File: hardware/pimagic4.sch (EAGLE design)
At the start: 49 parts, among them IC1 ATMEGA328-P, Q1 2N7000, Q2 2N7000, U2 ARDUINO_SHIELDLONGPADS, Y1 16MHz

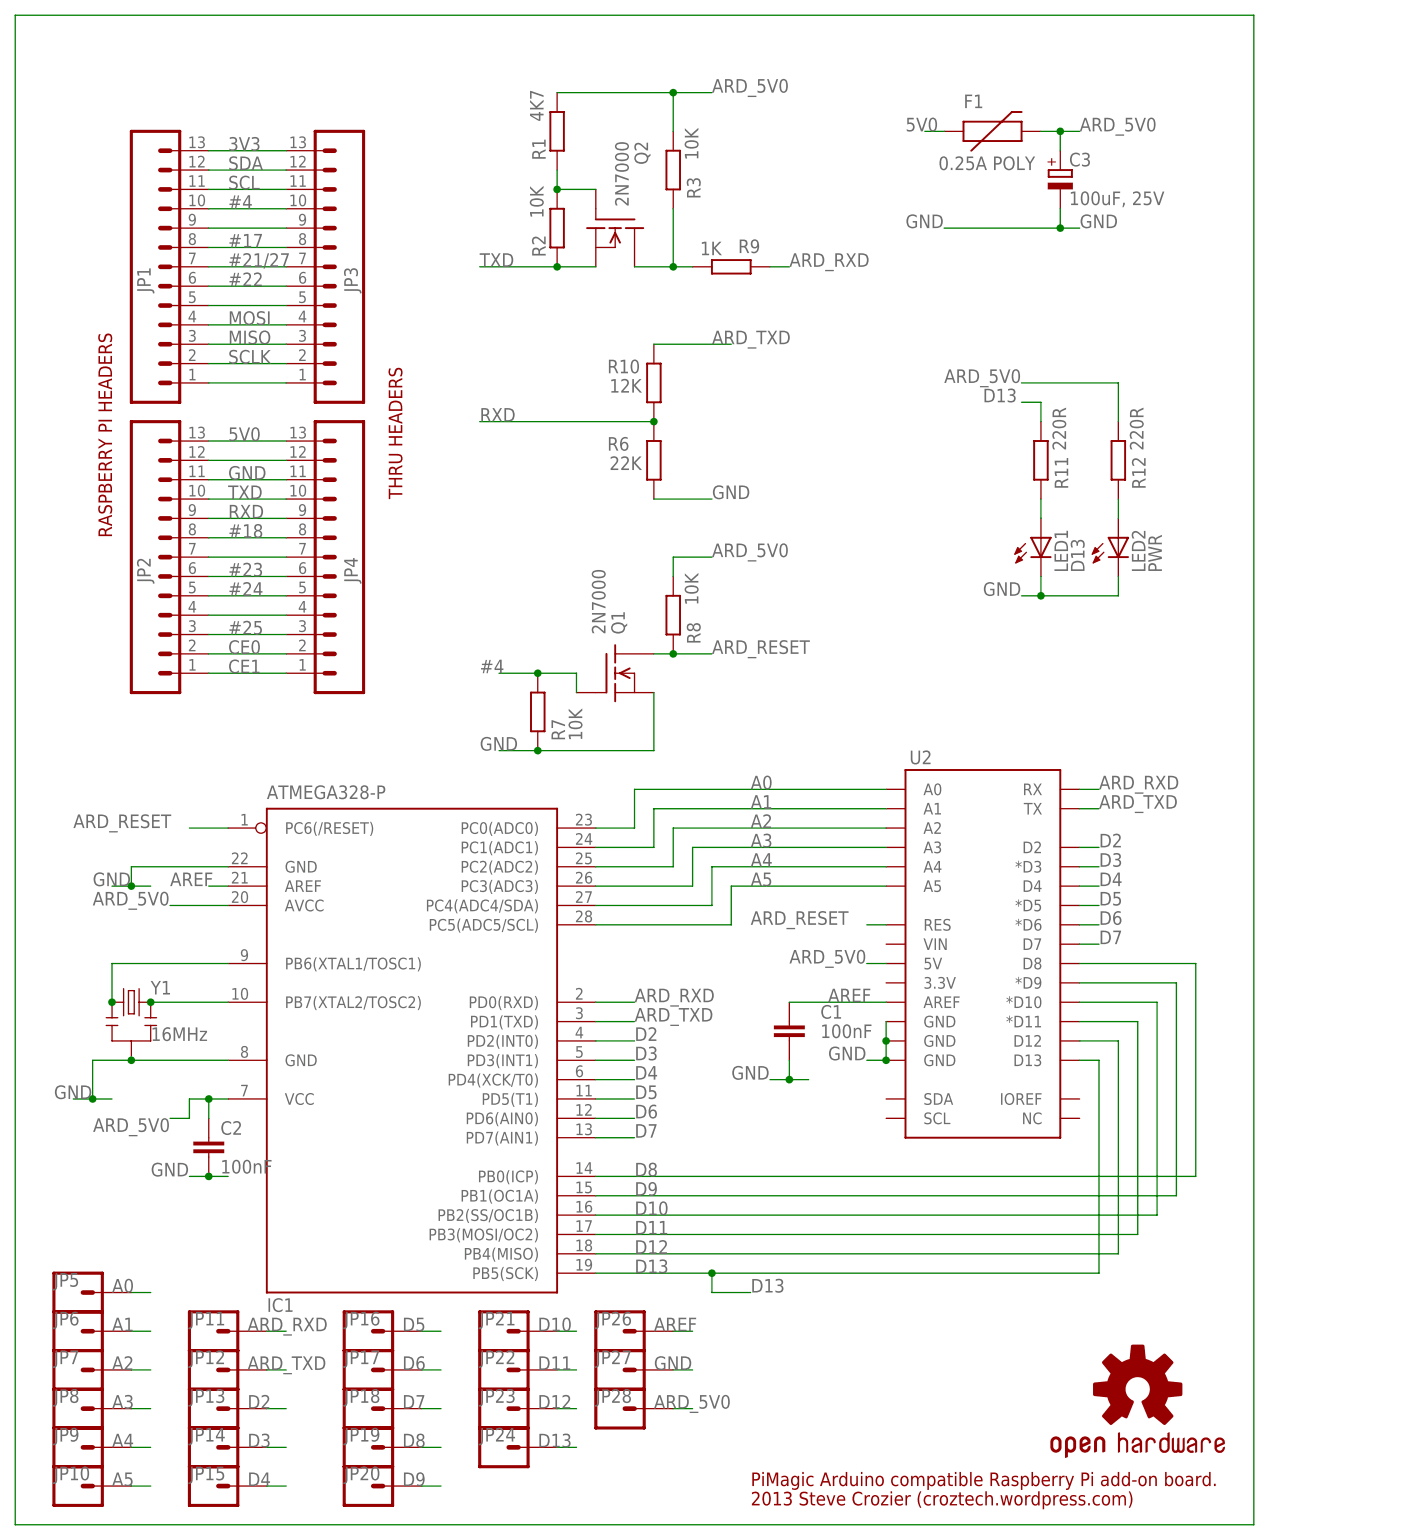
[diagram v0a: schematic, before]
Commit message: Rev01c update
- Q1/Q2 silkscreen corrected
- some of the silkscreen logos are now corrected
- there’s a nice ground plan copper pour added on both sides
- files updated to Eagle 7.1.0 format
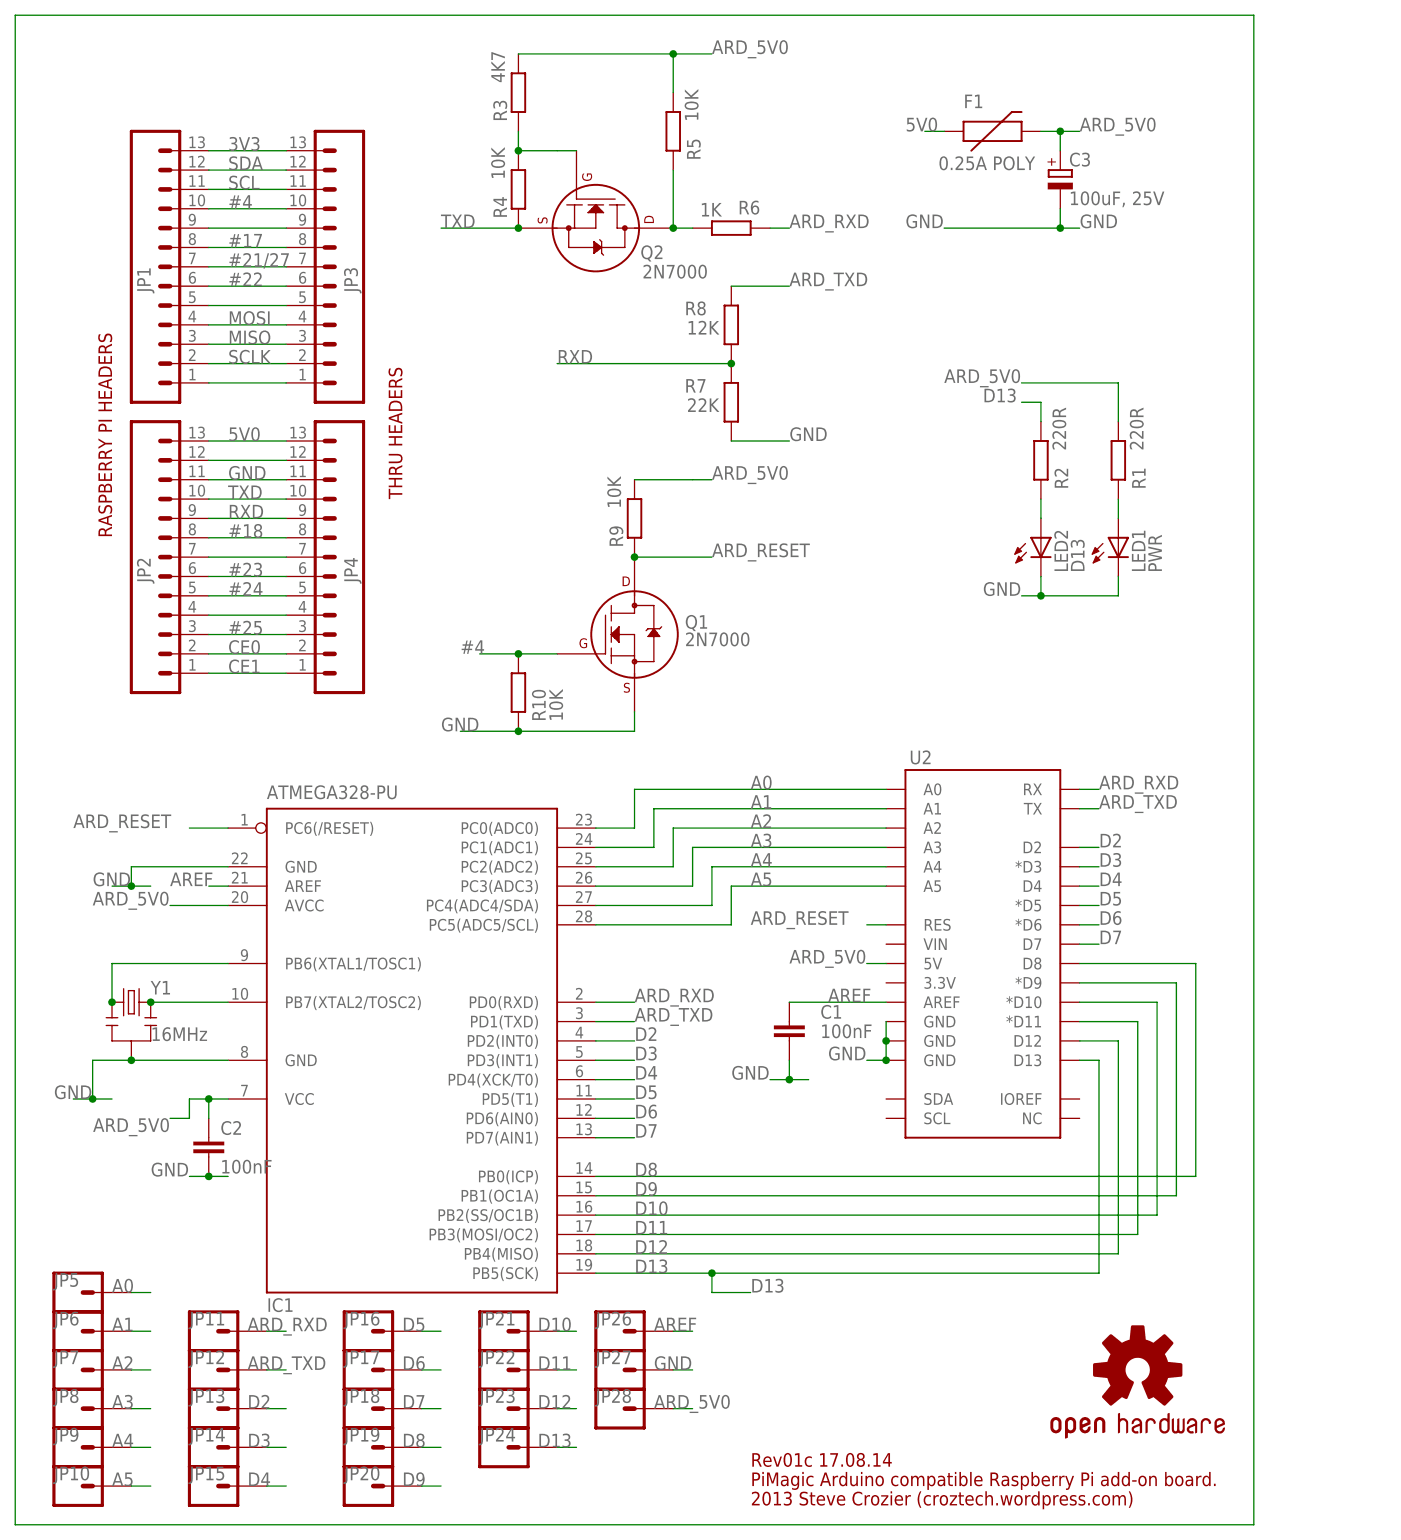
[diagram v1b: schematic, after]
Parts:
- removed R11, R12: 220R, resistor:R-EU_0207/10
- added R4, R5: 10K, resistor:R-EU_0207/10
- IC1: value ATMEGA328-P -> ATMEGA328-PU
- LED1: value D13 -> PWR
- LED2: value PWR -> D13
- Q1, Q2: device transistor-fet:BSS101 -> transistors:2N7000_TO92
- R1: value 4K7 -> 220R
- R10: value 12K -> 10K
- R2: value 10K -> 220R
- R3: value 10K -> 4K7
- R6: value 22K -> 1K
- R7: value 10K -> 22K
- R8: value 10K -> 12K
- R9: value 1K -> 10K
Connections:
- net #4: now also R10.2; no longer R7.2
- net ARD_5V0: now also R5.2, R9.2; no longer R12.2, R8.2
- net ARD_RESET: now also R9.1; no longer R8.1
- net ARD_RXD: now also R6.1; no longer R9.1
- net ARD_TXD: now also R8.1; no longer R10.1
- net D13: now also R2.2; no longer R11.2
- net GND: now also R10.1, R7.2; no longer R6.2, R7.1
- net N$10: now also LED2.A, R2.1; no longer LED1.A, R11.1
- net N$12: now also LED1.A, R1.1; no longer LED2.A, R12.1
- net N$3: now also R3.1, R4.2; no longer R1.1, R2.2
- net N$7: now also R5.1, R6.2; no longer R3.1, R9.2
- net RXD: now also R7.1, R8.2; no longer R10.2, R6.1
- net TXD: now also R4.1; no longer R2.1
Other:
- note added: "Rev01c 17.08.14"
- moved on the sheet: LED1, LED2, R1, R10, R2, R3, R6, R7, R8, R9
